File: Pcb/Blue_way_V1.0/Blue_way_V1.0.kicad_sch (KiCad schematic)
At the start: 0 parts

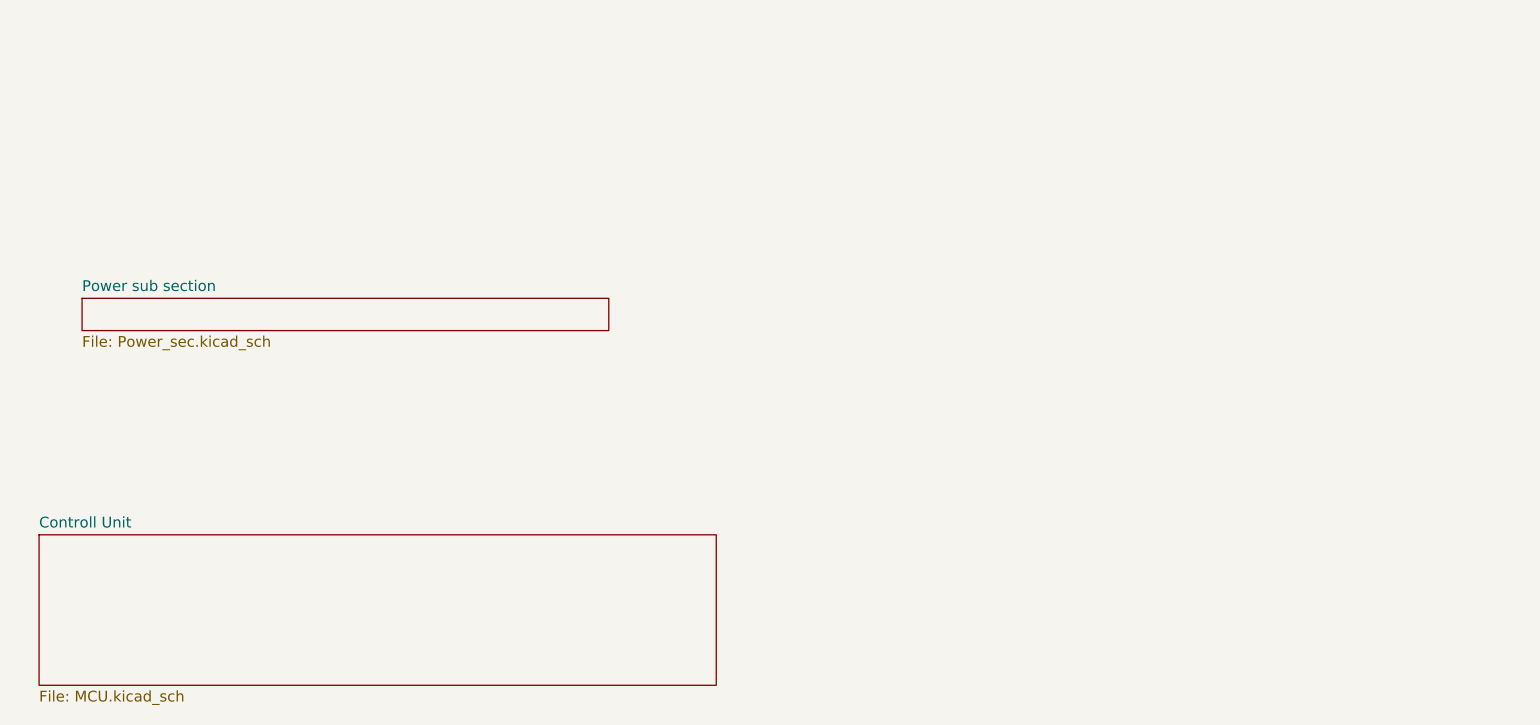
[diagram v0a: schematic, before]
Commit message: BNO085 Schematic updated
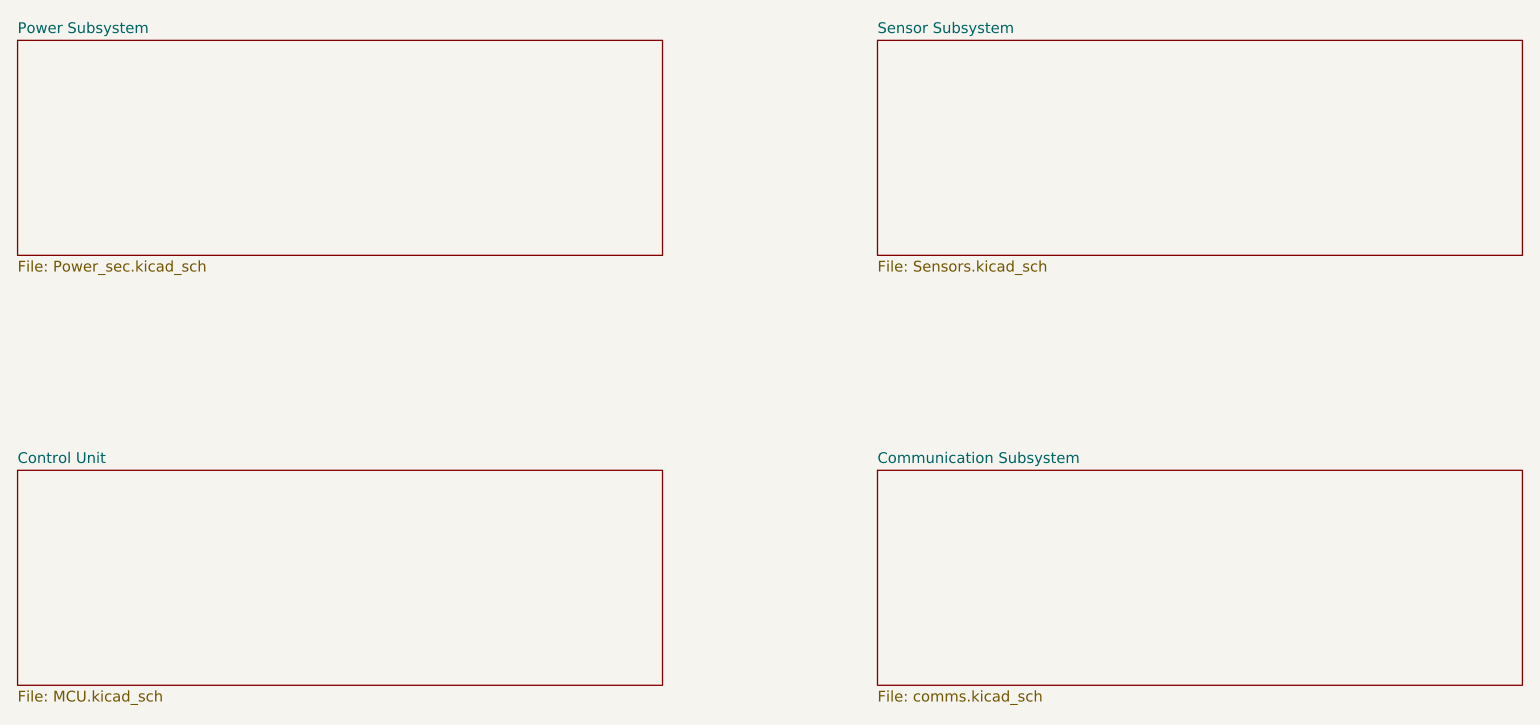
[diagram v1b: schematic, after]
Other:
- sheet Controll Unit renamed Control Unit
- sheet Power sub section renamed Power Subsystem
- added sheet Communication Subsystem (comms.kicad_sch)
- added sheet Sensor Subsystem (Sensors.kicad_sch)
- company: (none) -> BlueWay Horizon
- title: (none) -> Avionics Subsystem
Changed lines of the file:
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@@
 	(generator_version "9.0")
 	(paper "A4")
+	(title_block
+		(title "Avionics Subsystem")
+		(date "2026-03-05")
+		(rev "0.0.1")
+		(company "BlueWay Horizon")
+		(comment 1 "www.bluewayhorizon.in")
+	)
 	(sheet
-		(at 58.42 55.88)
-		(size 62.23 3.81)
+		(at 50.8 25.4)
+		(size 76.2 25.4)
 		(exclude_from_sim no)
 		(in_bom yes)
@@
 			(color 0 0 0 0.0000)
 		)
-		(property "Sheetname" "Power sub section"
-			(at 58.42 55.1684 0)
+		(property "Sheetname" "Power Subsystem"
+			(at 50.8 24.6884 0)
 			(effects
 				(font
@@
 		)
 		(property "Sheetfile" "Power_sec.kicad_sch"
-			(at 58.42 60.2746 0)
+			(at 50.8 51.3846 0)
 			(effects
 				(font
@@
 	)
 	(sheet
-		(at 53.34 83.82)
-		(size 80.01 17.78)
+		(at 152.4 25.4)
+		(size 76.2 25.4)
 		(exclude_from_sim no)
 		(in_bom yes)
@@
 			(color 0 0 0 0.0000)
 		)
-		(property "Sheetname" "Controll Unit"
-			(at 53.34 83.1084 0)
+		(property "Sheetname" "Sensor Subsystem"
+			(at 152.4 24.6884 0)
+			(effects
+				(font
+					(size 1.27 1.27)
+				)
+				(justify left bottom)
+			)
+		)
+		(property "Sheetfile" "Sensors.kicad_sch"
+			(at 152.4 51.3846 0)
+			(effects
+				(font
+					(size 1.27 1.27)
+				)
+				(justify left top)
+			)
+		)
+		(instances
+			(project "Blue_way_V1.0"
+				(path "/2f3247fa-a7e8-4139-878f-1aed25c1e4d8"
+					(page "4")
+				)
+			)
+		)
+	)
+	(sheet
+		(at 152.4 76.2)
+		(size 76.2 25.4)
+		(exclude_from_sim no)
+		(in_bom yes)
+		(on_board yes)
+		(dnp no)
+		(fields_autoplaced yes)
+		(stroke
+			(width 0.1524)
+			(type solid)
+		)
+		(fill
+			(color 0 0 0 0.0000)
+		)
+		(property "Sheetname" "Communication Subsystem"
+			(at 152.4 75.4884 0)
+			(effects
+				(font
+					(size 1.27 1.27)
+				)
+				(justify left bottom)
+			)
+		)
+		(property "Sheetfile" "comms.kicad_sch"
+			(at 152.4 102.1846 0)
+			(effects
+				(font
+					(size 1.27 1.27)
+				)
+				(justify left top)
+			)
+		)
+		(instances
+			(project "Blue_way_V1.0"
+				(path "/2f3247fa-a7e8-4139-878f-1aed25c1e4d8"
+					(page "5")
+				)
+			)
+		)
+	)
+	(sheet
+		(at 50.8 76.2)
+		(size 76.2 25.4)
+		(exclude_from_sim no)
+		(in_bom yes)
+		(on_board yes)
+		(dnp no)
+		(fields_autoplaced yes)
+		(stroke
+			(width 0.1524)
+			(type solid)
+		)
+		(fill
+			(color 0 0 0 0.0000)
+		)
+		(property "Sheetname" "Control Unit"
+			(at 50.8 75.4884 0)
 			(effects
 				(font
@@
 		)
 		(property "Sheetfile" "MCU.kicad_sch"
-			(at 53.34 102.1846 0)
+			(at 50.8 102.1846 0)
 			(effects
 				(font
